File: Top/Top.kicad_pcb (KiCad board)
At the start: 2 copper layers, 40 x 40 mm, 31 parts, among them J1 Conn_01x02_Male, SW1 SW_DPDT_x2, U2 MCP73831-2-OT, U3 SSD1306

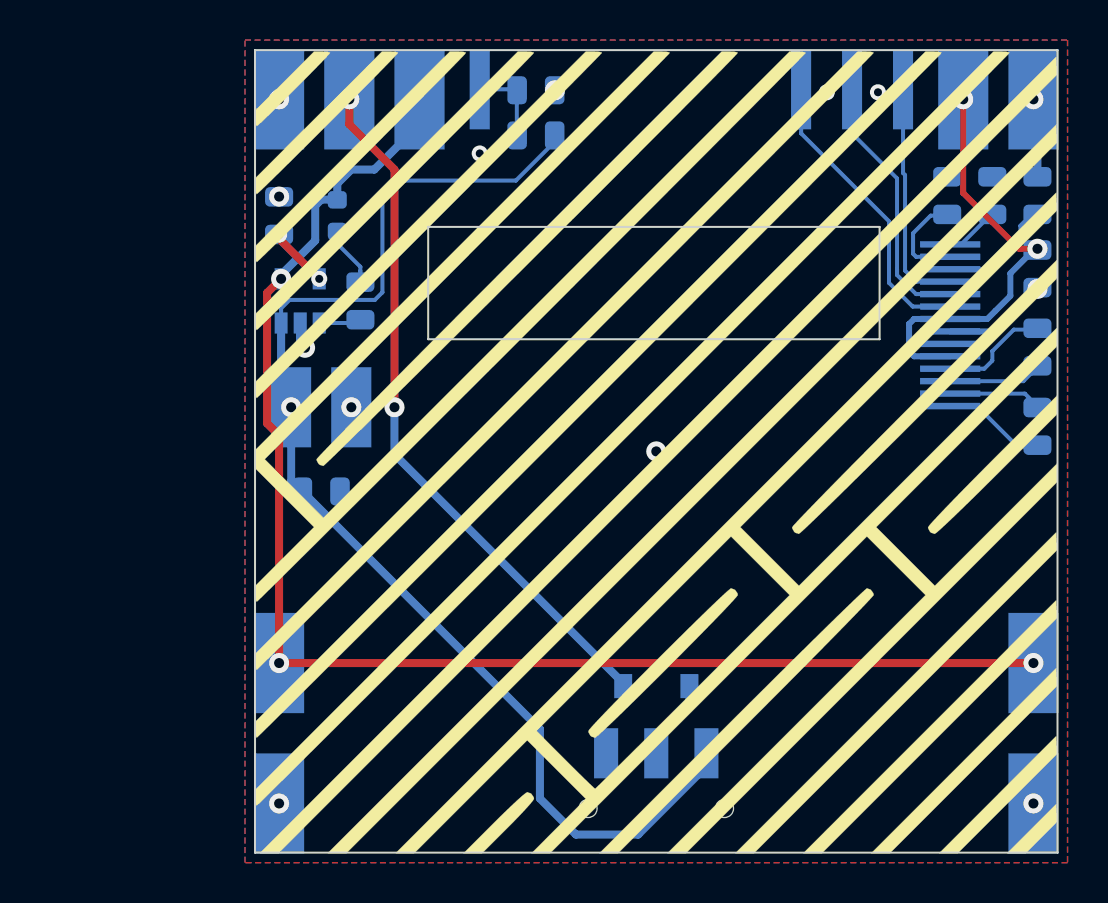
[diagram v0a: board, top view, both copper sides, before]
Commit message: updated bottom (motor placement, sharp sensor), front redesign, start op top redesign
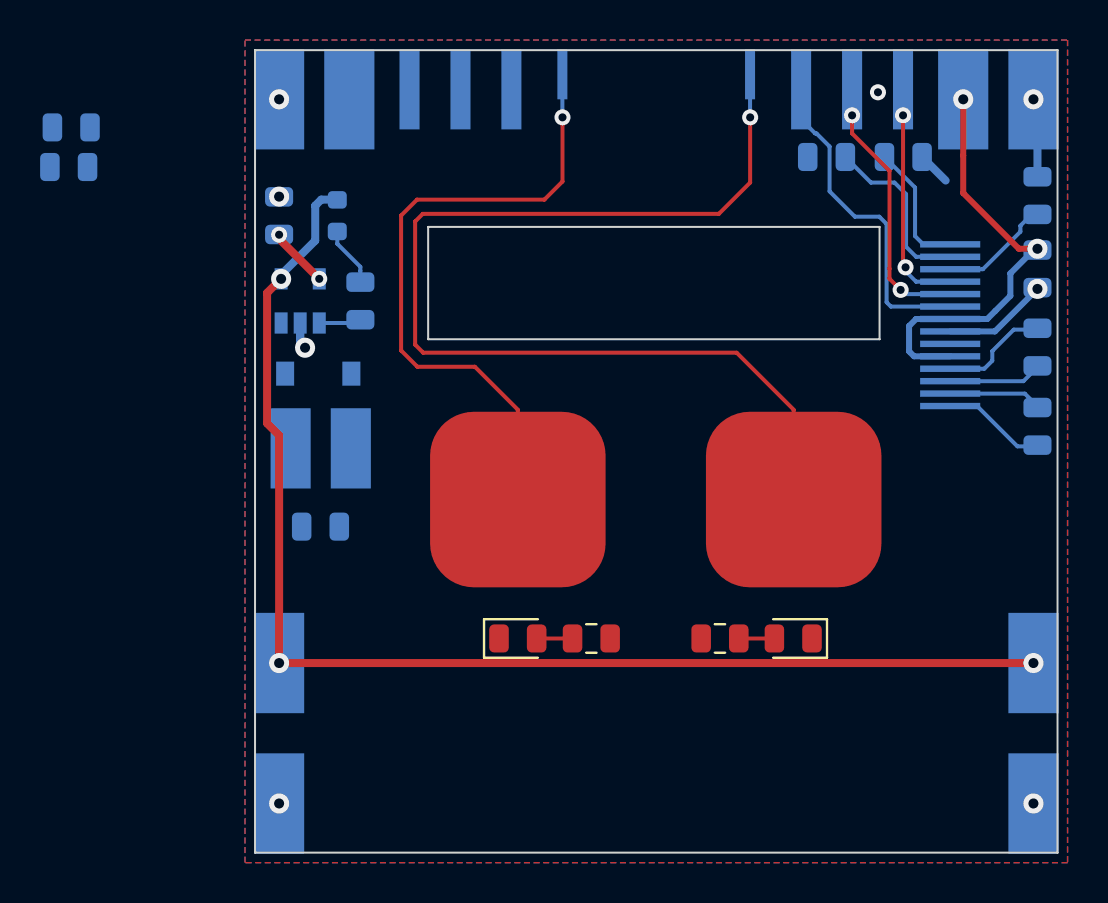
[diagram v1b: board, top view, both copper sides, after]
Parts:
- removed G***: LOGO, Print:d3
- removed SW1: SW_DPDT_x2, Custom:JS102011SAQN
- added D3: GRN, LED_SMD:LED_0805_2012Metric, F.Cu at (143.6, 124.8)
- added D4: BLU, LED_SMD:LED_0805_2012Metric, F.Cu at (157.3, 124.8)
- added H14: LED2, Custom:Mounting_Pad_Signal, B.Cu at (143.3, 97.5)
- added H15: TCH1, Custom:Mounting_Pad_Touch, B.Cu at (145.8, 96.7)
- added H16: PAD1, Custom:Touch_Pad, F.Cu at (143.6, 117.9)
- added H17: TCH2, Custom:Mounting_Pad_Touch, B.Cu at (155.2, 96.7)
- added H18: PAD2, Custom:Touch_Pad, F.Cu at (157.3, 117.9)
- added R6: 150, Resistor_SMD:R_0805_2012Metric, F.Cu at (147.3, 124.8)
- added R7: 150, Resistor_SMD:R_0805_2012Metric, F.Cu at (153.7, 124.8)
- H12, H13: value VBS -> PWR
- H2: value VSW -> PWR
- H3: value ORES -> O~RST
- H6: value VBS -> LED1; footprint Custom:Mounting_Pad_Power -> Custom:Mounting_Pad_Signal
- moved R1 23.3 mm to (121.2, 101.3)
- moved R2 23.2 mm to (121.3, 99.3)
- moved D1 22.9 mm to (133.7, 111.6), turned to 180 degrees
- moved C6 6.31 mm to (159.0, 100.8), turned to 180 degrees
- moved C7 4.84 mm to (162.8, 100.8), turned to 180 degrees
- moved H1 3.50 mm to (138.2, 97.5)
- moved H6 2.10 mm to (140.7, 97.5)
- moved J1 2.05 mm to (133.8, 117.3)
- moved C2 1.75 mm to (133.8, 119.2)
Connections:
- D1 pad 1: /VBAT_SWITCH -> VBUS
- D1 pad 2: Net-(D1-Pad2) -> +BATT
- H2 pad 1: /VBAT_SWITCH -> VBUS
- H6 pad 1: VBUS -> Net-(H6-Pad1)
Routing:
- net +BATT: track 60.9 -> 0.00 mm, vias 1 -> 0
- net /T2: track 0.00 -> 53.7 mm, vias 0 -> 1
- net /VBAT_SWITCH: track 34.9 -> 0.00 mm, vias 2 -> 0
- net /T1: track 0.00 -> 32.3 mm, vias 0 -> 1
- net VBUS: track 71.9 -> 62.9 mm
- net /BAT_MON: track 4.12 -> 0.00 mm
- net Net-(D1-Pad2): track 4.03 -> 0.00 mm
- net Net-(C6-Pad1): track 5.00 -> 8.82 mm
- net Net-(C7-Pad2): track 2.69 -> 6.50 mm
- net Net-(D3-Pad2): track 0.00 -> 1.79 mm
- net Net-(D4-Pad2): track 0.00 -> 1.77 mm
- net GND: track 11.6 -> 13.3 mm, vias 13 -> 8
- net /OLED_SDA: track 11.6 -> 10.3 mm, vias 0 -> 2
- net /OLED_SCL: track 13.5 -> 12.3 mm, vias 0 -> 2
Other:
- net class Touch added: clearance 0.5, trace_width 0.2, via_dia 0.8, via_drill 0.4
- board text added: "Cuby V0.2"
- board text removed: "Cuby V0.1"

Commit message: Update Top V0.2, small changes to motor placement
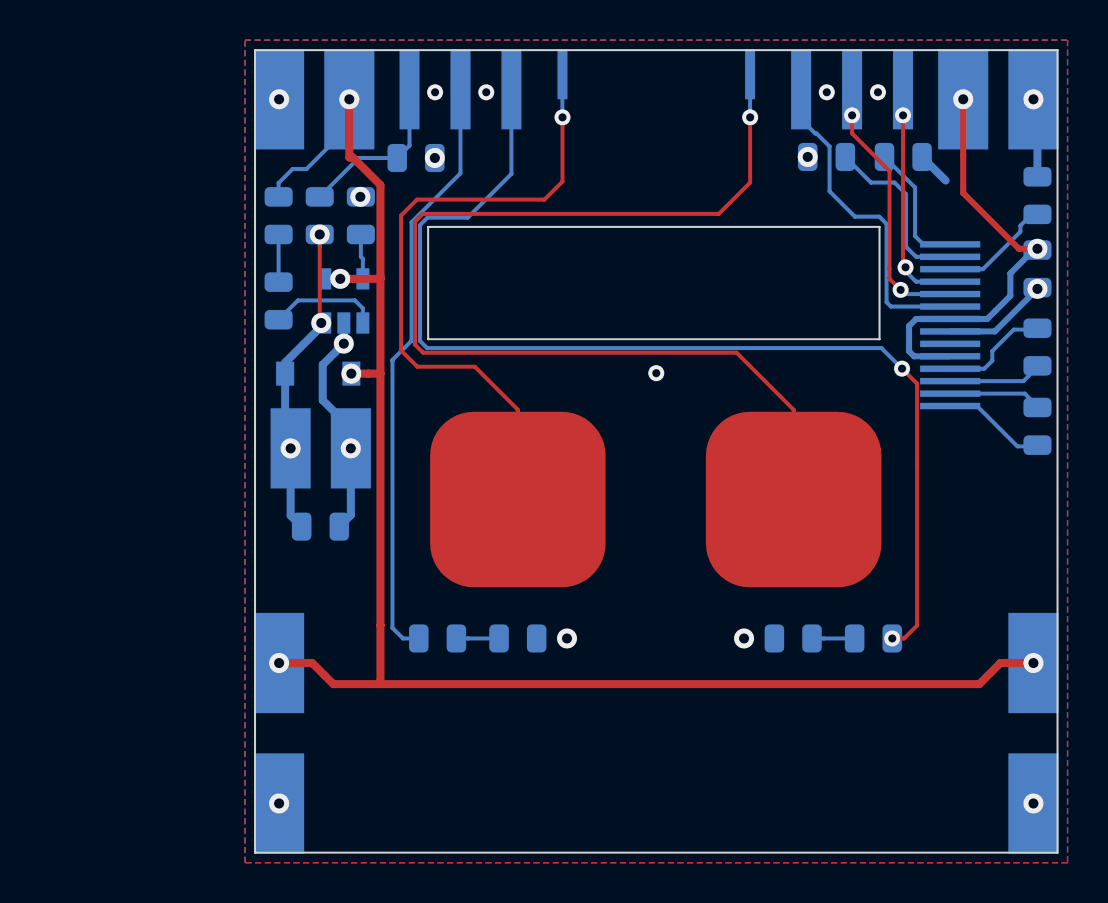
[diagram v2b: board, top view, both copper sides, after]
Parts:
- D2: footprint LED_SMD:LED_0603_1608Metric -> LED_SMD:LED_0805_2012Metric
- D3, D4, R6, R7: moved to B.Cu
- moved R2 17.3 mm to (138.5, 100.9)
- moved H16 13.8 mm to (157.3, 117.9)
- moved H18 13.8 mm to (143.6, 117.9)
- moved R1 12.7 mm to (133.7, 103.8), turned to 90 degrees
- moved H15 9.36 mm to (155.2, 96.7)
- moved H17 9.35 mm to (145.8, 96.7)
- moved R6 7.66 mm to (139.6, 124.8), turned to 0 degrees
- moved R7 7.65 mm to (161.3, 124.8), turned to 180 degrees
- moved R4 4.08 mm to (135.8, 103.8)
- moved R3 4.07 mm to (131.7, 108.0)
- moved D2 2.92 mm to (131.7, 103.8)
- moved U2 2.18 mm to (134.9, 108.0)
- turned D3 to 180 degrees
- turned D4 to 0 degrees
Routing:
- net Net-(H14-Pad1): track 0.00 -> 54.8 mm, vias 0 -> 2
- net Net-(H6-Pad1): track 0.00 -> 29.8 mm
- net /T2: track 53.7 -> 32.3 mm
- net /T1: track 32.3 -> 53.7 mm
- net +BATT: track 0.00 -> 16.5 mm, vias 0 -> 3
- net VBUS: track 62.9 -> 79.4 mm, vias 3 -> 5
- net GND: track 13.3 -> 23.1 mm, vias 8 -> 17
- net /BAT_MON: track 0.00 -> 8.34 mm
- net Net-(R3-Pad2): track 2.11 -> 5.49 mm
- net Net-(R4-Pad1): track 3.03 -> 2.25 mm, vias 2 -> 0
- net Net-(D2-Pad1): track 2.98 -> 2.38 mm
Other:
- board text added: "+"
- board text added: "-"

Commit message: finish top, changes to front, added graphic
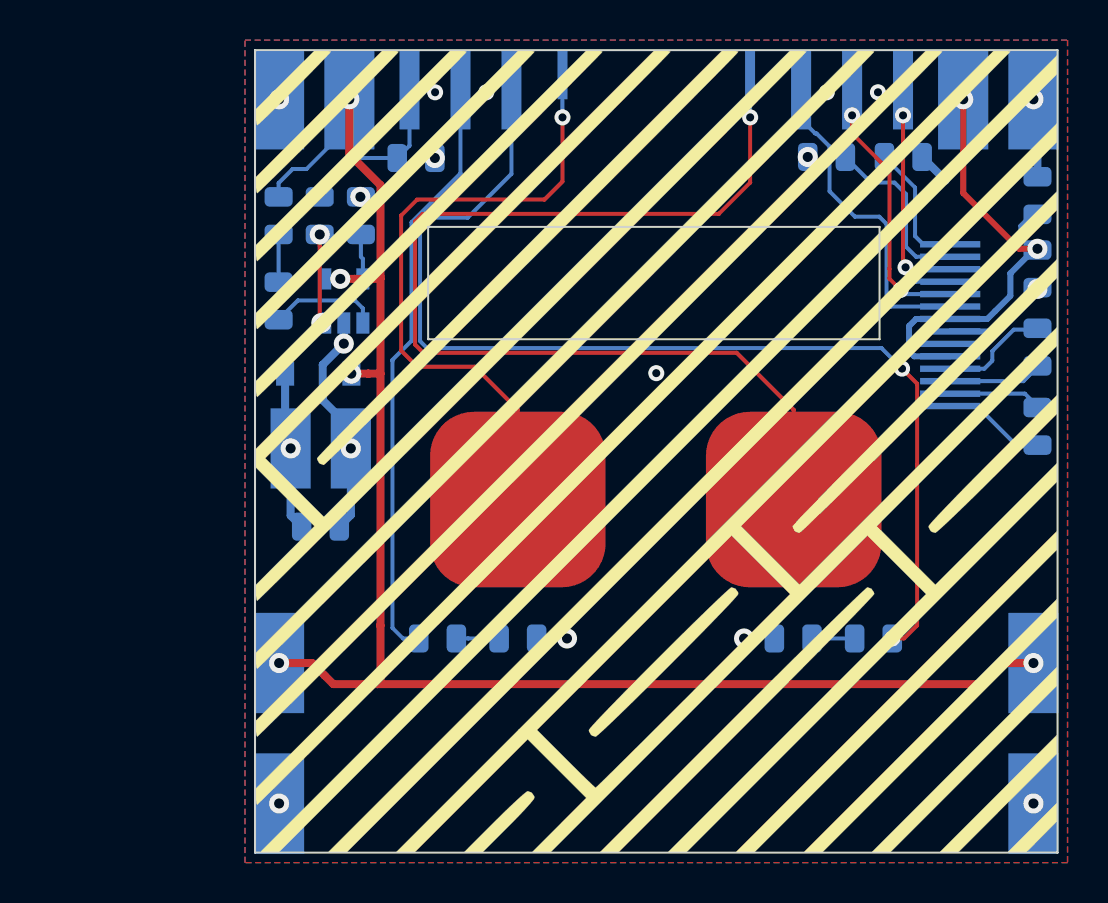
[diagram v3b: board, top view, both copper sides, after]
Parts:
- added G1: Graphic, Print:d3, F.Cu at (150.5, 115.5)

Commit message: finishing touches, moved touch traces to back
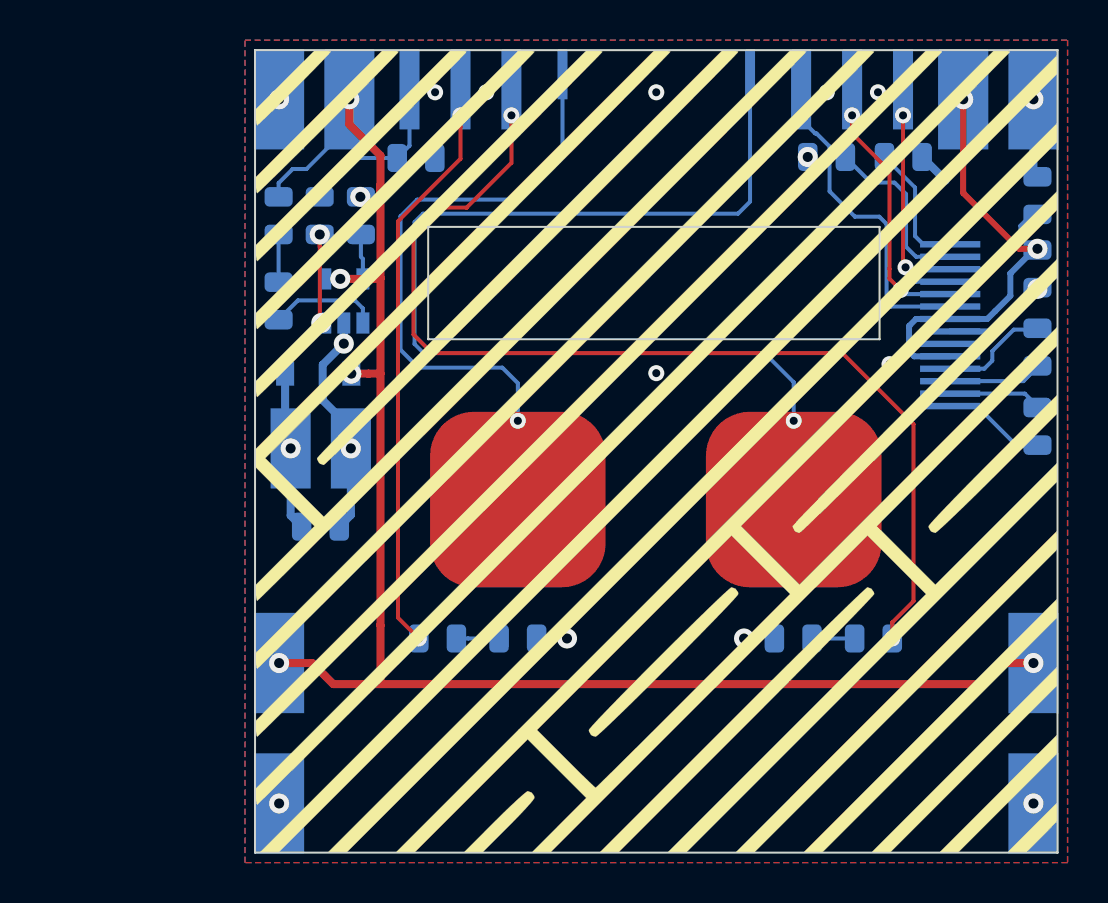
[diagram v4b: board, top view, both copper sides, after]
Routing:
- net /T2: track 32.3 -> 28.3 mm
- net Net-(H14-Pad1): track 54.8 -> 51.7 mm
- net /T1: track 53.7 -> 51.2 mm
- net Net-(H6-Pad1): track 29.8 -> 27.8 mm, vias 0 -> 2
- net VBUS: track 79.4 -> 78.6 mm
- net GND: track 23.1 -> 23.5 mm, vias 17 -> 18
